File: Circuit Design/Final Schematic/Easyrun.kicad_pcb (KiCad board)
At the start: 2 copper layers, 100.4 x 94.2 mm, 78 parts, among them U1 ESP32-WROOM-32

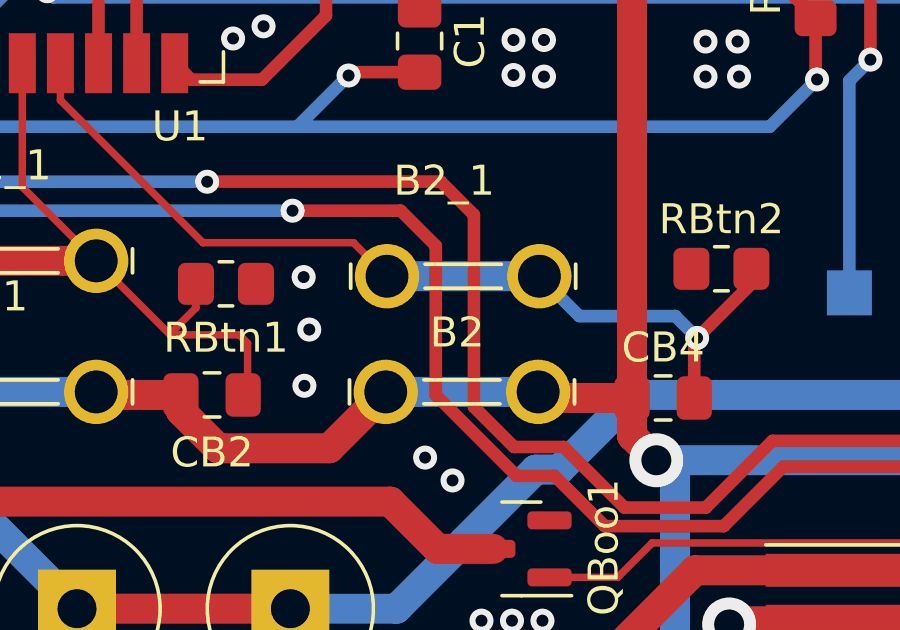
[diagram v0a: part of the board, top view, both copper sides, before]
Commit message: Updated values on PCB
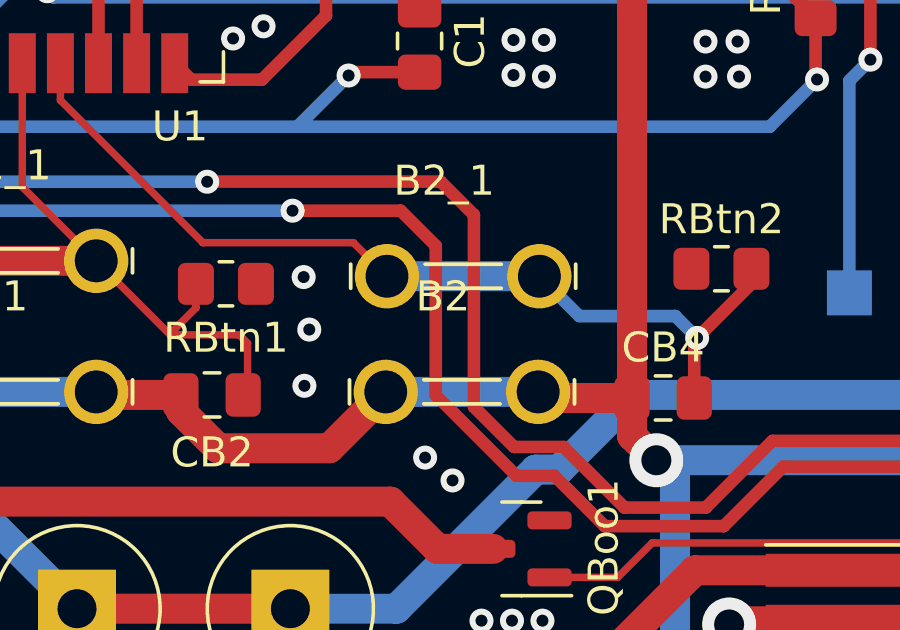
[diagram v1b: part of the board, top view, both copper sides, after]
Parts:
- Crec1: value 100u -> 470u
- Lrec1: value 440m -> 250m

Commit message: New transformer
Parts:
- Lrec1: value 250m -> 150m

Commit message: Buck converters simmulations
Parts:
- CB3, CB5: value 22u -> 47u
- C_b1: value C_Polarized -> 47u
